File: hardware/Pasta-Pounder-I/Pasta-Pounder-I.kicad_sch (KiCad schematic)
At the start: 9 parts, among them CN1 XT30UPB-M, J1 USB_C_Receptacle, U2 DRV8874PWPR, U3 DRV8874PWPR, U4 USBLC6-2P6, U5 ESP32-S3-WROOM-1

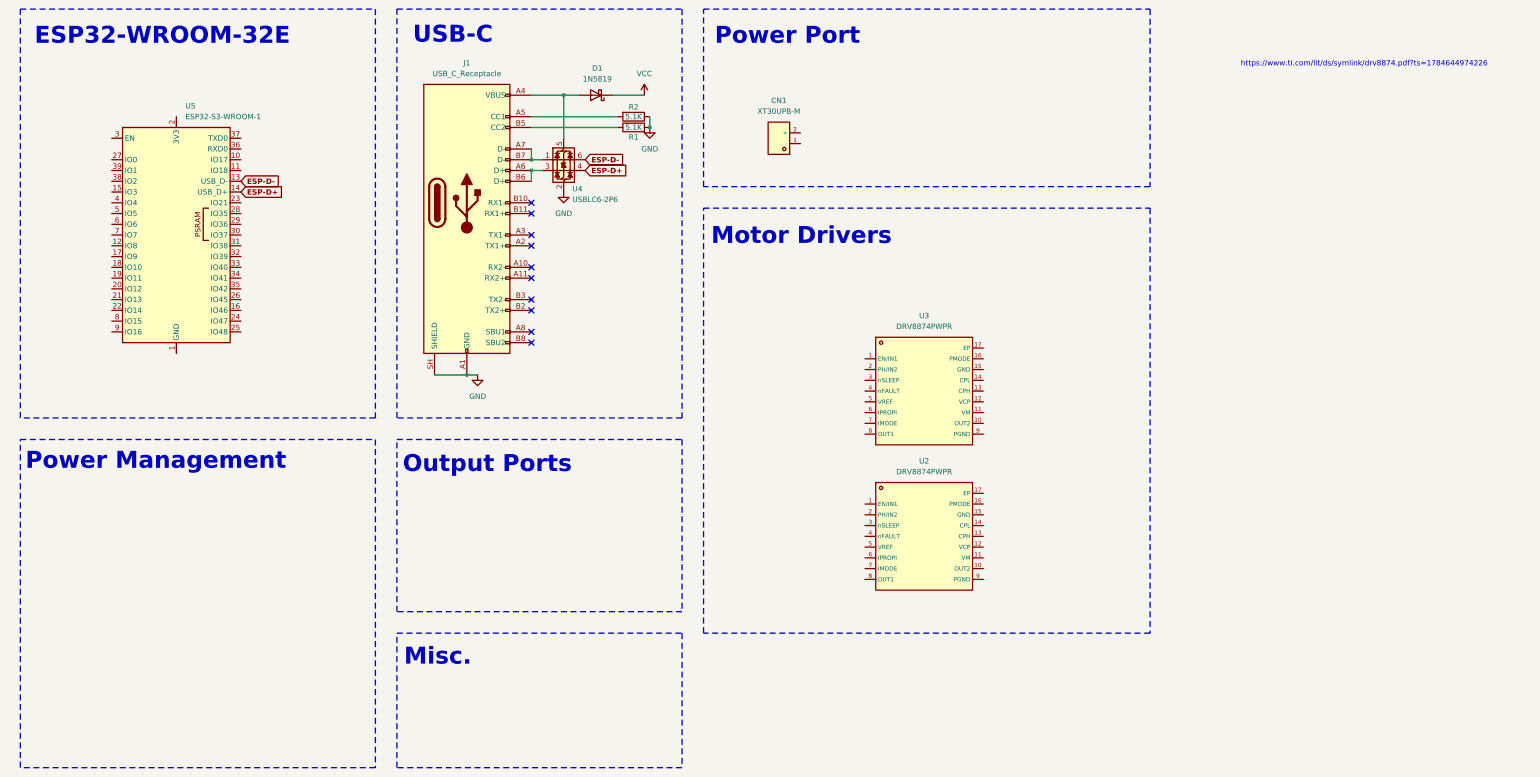
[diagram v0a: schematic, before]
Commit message: Finished esp32 schematic
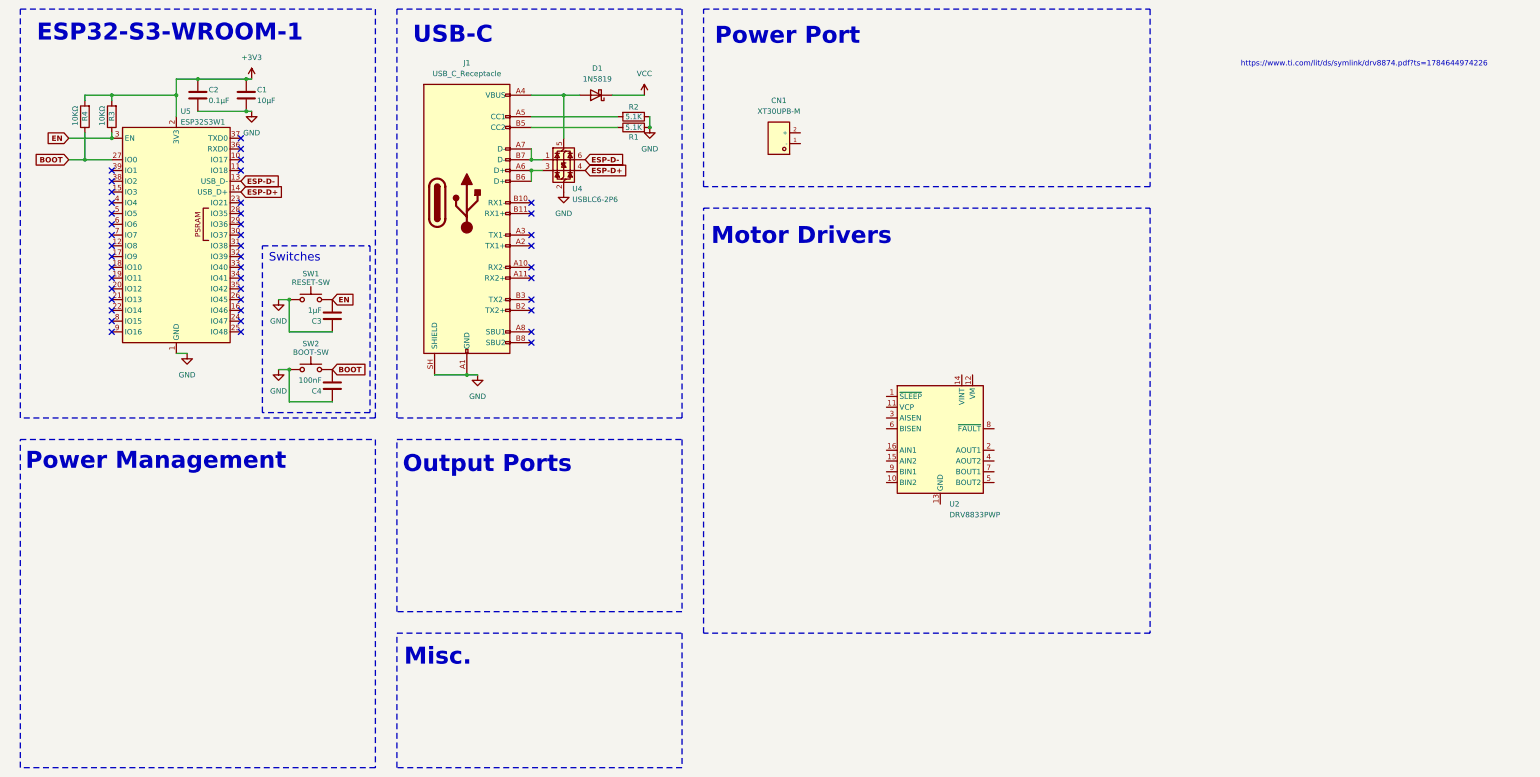
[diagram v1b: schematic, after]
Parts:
- removed U2, U3: DRV8874PWPR, lcsc_footprints:C1855818_HTSSOP-16_L5_0-W4_4-P0_65-LS6_4-BL-EP, symbol lcsc_imported:DRV8874PWPR
- added C1: 10µF, symbol Device:C
- added C2: 0.1µF, symbol Device:C
- added C3: 1µF, symbol Device:C
- added C4: 100nF, symbol Device:C
- added R3, R4: 10KΩ, symbol Device:R
- added SW1: RESET-SW, symbol Switch:SW_Push
- added SW2: BOOT-SW, symbol Switch:SW_Push
- added U2: DRV8833PWP, Package_SO:HTSSOP-16-1EP_4.4x5mm_P0.65mm_EP3.4x5mm_Mask2.46x2.31mm_ThermalVias, symbol Driver_Motor:DRV8833PWP
- U5: value ESP32-S3-WROOM-1 -> ESP32S3W1
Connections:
- net GND: now also U5.1 (GND), U5.40 (GND), U5.41 (GND), C1.2, C2.2, C3.1, C4.1, SW1.1, SW2.1
- net +3V3: now reaches U5.2 (3V3)
- net +3V3: now also C1.1, C2.1, R3.2, R4.2
- net BOOT: now reaches U5.27 (IO0)
- net BOOT: now also C4.2, R4.1, SW2.2
- net EN: now reaches U5.3 (EN)
- net EN: now also C3.2, R3.1, SW1.2
- new net: U2.13 (GND), U2.17 (GND)
- no-connect marks 10 -> 43
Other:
- note added: "ESP32-S3-WROOM-1"
- note added: "Switches"
- note removed: "ESP32-WROOM-32E"

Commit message: Finished Motor Schematic
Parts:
- removed U2: DRV8833PWP, Package_SO:HTSSOP-16-1EP_4.4x5mm_P0.65mm_EP3.4x5mm_Mask2.46x2.31mm_ThermalVias, symbol Driver_Motor:DRV8833PWP
- added C10, C5: 0.022µF, symbol Device:C
- added C11, C6, C7, C9: 0.1µF, symbol Device:C
- added C12, C8: 470µF, symbol Device:C
- added J2: Brushed_Motor_1, symbol Connector:Screw_Terminal_01x02
- added J3: Brushed_Motor_2, symbol Connector:Screw_Terminal_01x02
- added R10, R7: 50KΩ, symbol Device:R
- added R5, R8: 10KΩ, symbol Device:R
- added R6, R9: 16KΩ, symbol Device:R
- added U1, U2: DRV8874PWPR, lcsc_footprints:C1855818_HTSSOP-16_L5_0-W4_4-P0_65-LS6_4-BL-EP, symbol lcsc_imported:DRV8874PWPR
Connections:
- net +3V3: now also R5.1, R6.1, R8.1, R9.1
- net GND: now also C11.1, C12.1, C7.1, C8.1, R10.2, R7.2, U1.15 (GND), U1.16 (PMODE), U1.17 (EP), U1.7 (IMODE), U1.9 (PGND), U2.15 (GND), U2.16 (PMODE), U2.17 (EP), U2.7 (IMODE), U2.9 (PGND)
- net VCC: now also C11.2, C12.2, C6.2, C7.2, C8.2, C9.2, U1.11 (VM), U2.11 (VM)
- new net: J2.1 (Pin_1), U1.10 (OUT2)
- new net: J2.2 (Pin_2), U1.8 (OUT1)
- new net: J3.1 (Pin_1), U2.10 (OUT2)
- new net: J3.2 (Pin_2), U2.8 (OUT1)
- new net: C10.1, U2.14 (CPL)
- new net: C10.2, U2.13 (CPH)
- new net: C5.1, U1.14 (CPL)
- new net: C5.2, U1.13 (CPH)
- new net: C9.1, U2.12 (VCP)
- new net: C6.1, U1.12 (VCP)
- new net DRV1-EN: U1.1 (EN/IN1)
- new net DRV1-IPROPI: R5.2, U1.6 (IPROPI)
- new net DRV1-PH: U1.2 (PH/IN2)
- new net DRV1-VREF: R6.2, R7.1, U1.5 (VREF)
- new net DRV1-nFAULT: U1.4 (nFAULT)
- new net DRV1-nSLEEP: U1.3 (nSLEEP)
- new net DRV2-EN: U2.1 (EN/IN1)
- new net DRV2-IPROPI: R8.2, U2.6 (IPROPI)
- new net DRV2-PH: U2.2 (PH/IN2)
- new net DRV2-VREF: R10.1, R9.2, U2.5 (VREF)
- new net DRV2-nFAULT: U2.4 (nFAULT)
- new net DRV2-nSLEEP: U2.3 (nSLEEP)
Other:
- moved on the sheet: CN1

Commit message: Finished Power Port Schematic
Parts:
- added C13: C_Polarized, symbol Device:C_Polarized
- added D2: Z5V6, PCM_JLCPCB:D_SOD-123, symbol PCM_JLCPCB-Diodes:Zener,MM1Z5V6
- added Q1: AO3401A, Package_TO_SOT_SMD:SOT-23, symbol Transistor_FET:AO3401A
- added R11: R, symbol Device:R
- added SW3: 5.8 ZSPT, lcsc_footprints:C2681588_SW-TH_5_8ZSPT, symbol lcsc_imported:5_8_ZSPT
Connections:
- net GND: now also CN1.1 (-), C13.2, R11.2
- net VCC: now also C13.1, D2.1, Q1.2 (S)
- net at CN1.2 (+): now also SW3.3
- new net: Q1.3 (D), SW3.2
- new net: D2.2, Q1.1 (G), R11.1
- no-connect marks 43 -> 47
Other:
- company: (none) -> Team Carbonara
- moved on the sheet: CN1
